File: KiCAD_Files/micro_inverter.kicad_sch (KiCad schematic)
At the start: 47 parts, among them J1 Conn_01x01, J103 B2B-EH-A(LF)(SN), J104 B2B-EH-A(LF)(SN), J105 B2B-EH-A(LF)(SN), J2 Conn_01x01, J3 Conn_01x01, J7 Conn_01x01, J8 Conn_01x01, K1 G2RL-1A-H, K2 G2RL-2A, Q501 IPD60R210PFD7SAUMA1, Q502 IPD60R210PFD7SAUMA1, Q503 IPD60R210PFD7SAUMA1, Q504 IPD60R210PFD7SAUMA1, Q505 IPD60R210PFD7SAUMA1, Q506 IPD60R210PFD7SAUMA1, Q507 IPD60R210PFD7SAUMA1, Q508 IPD60R210PFD7SAUMA1, Q509 IPD60R210PFD7SAUMA1, Q510 IPD60R210PFD7SAUMA1, Q511 IPD60R210PFD7SAUMA1, Q512 IPD60R210PFD7SAUMA1, T1 Transformer_1P_1S

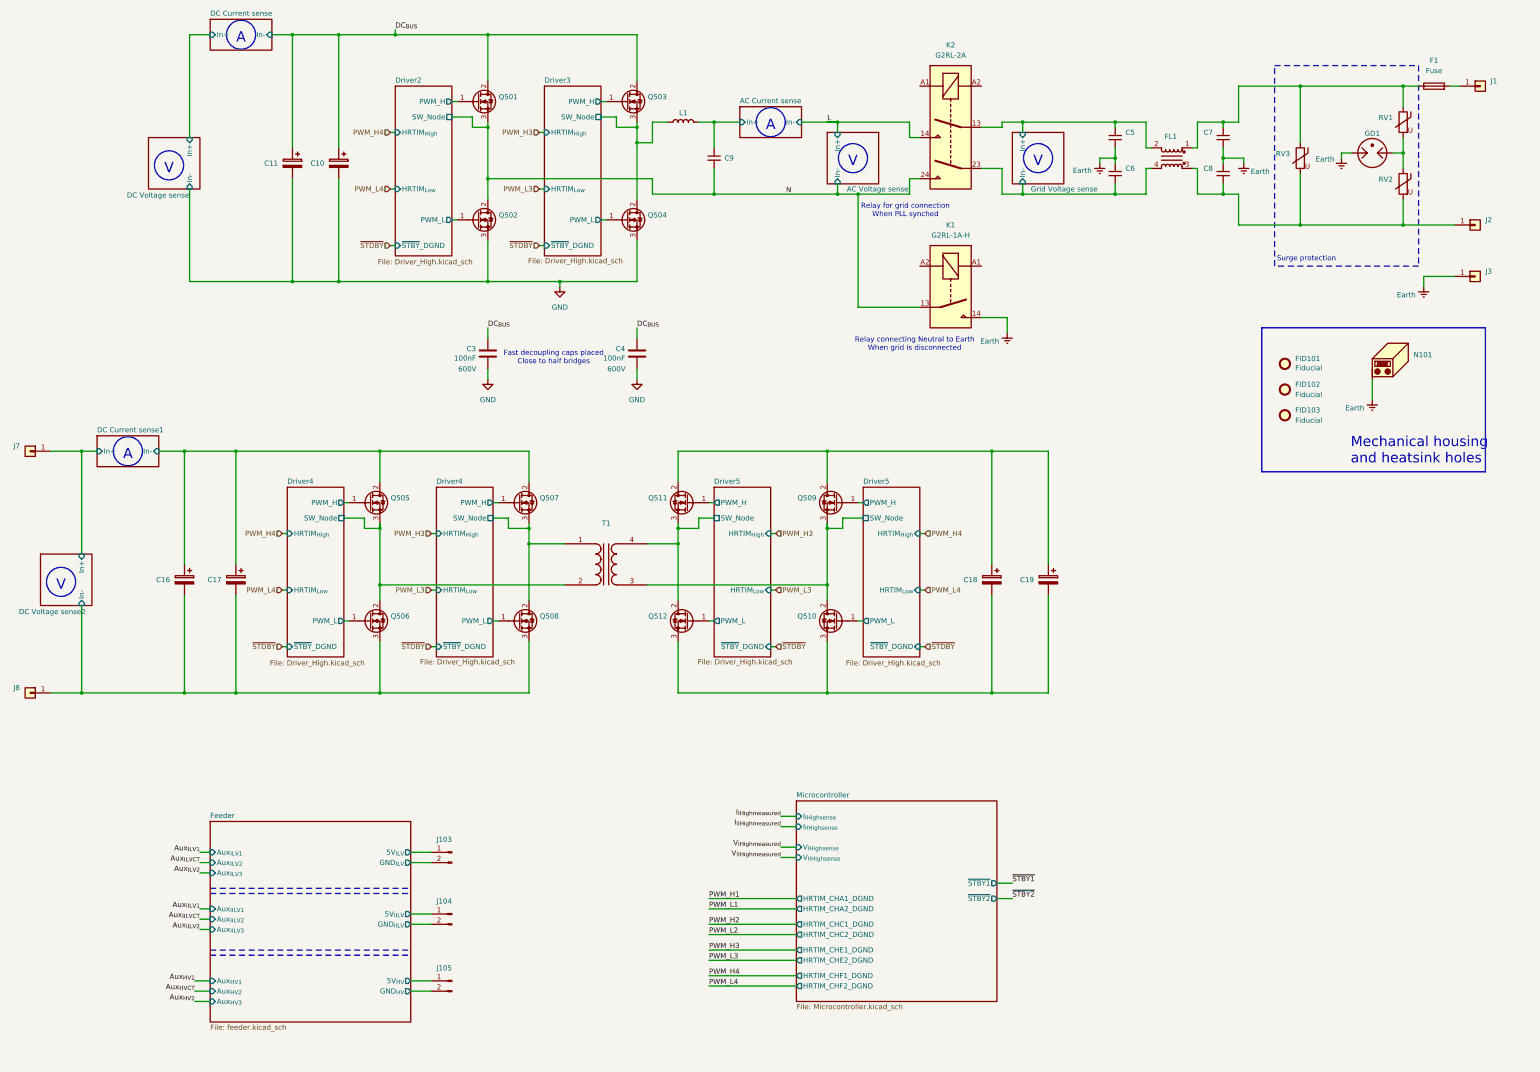
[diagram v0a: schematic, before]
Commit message: Changed the architecture from DAB to full-bridge. Added low side feeder.
Signed-off-by: Jean Alinei <jean.alinei@owntech.org>
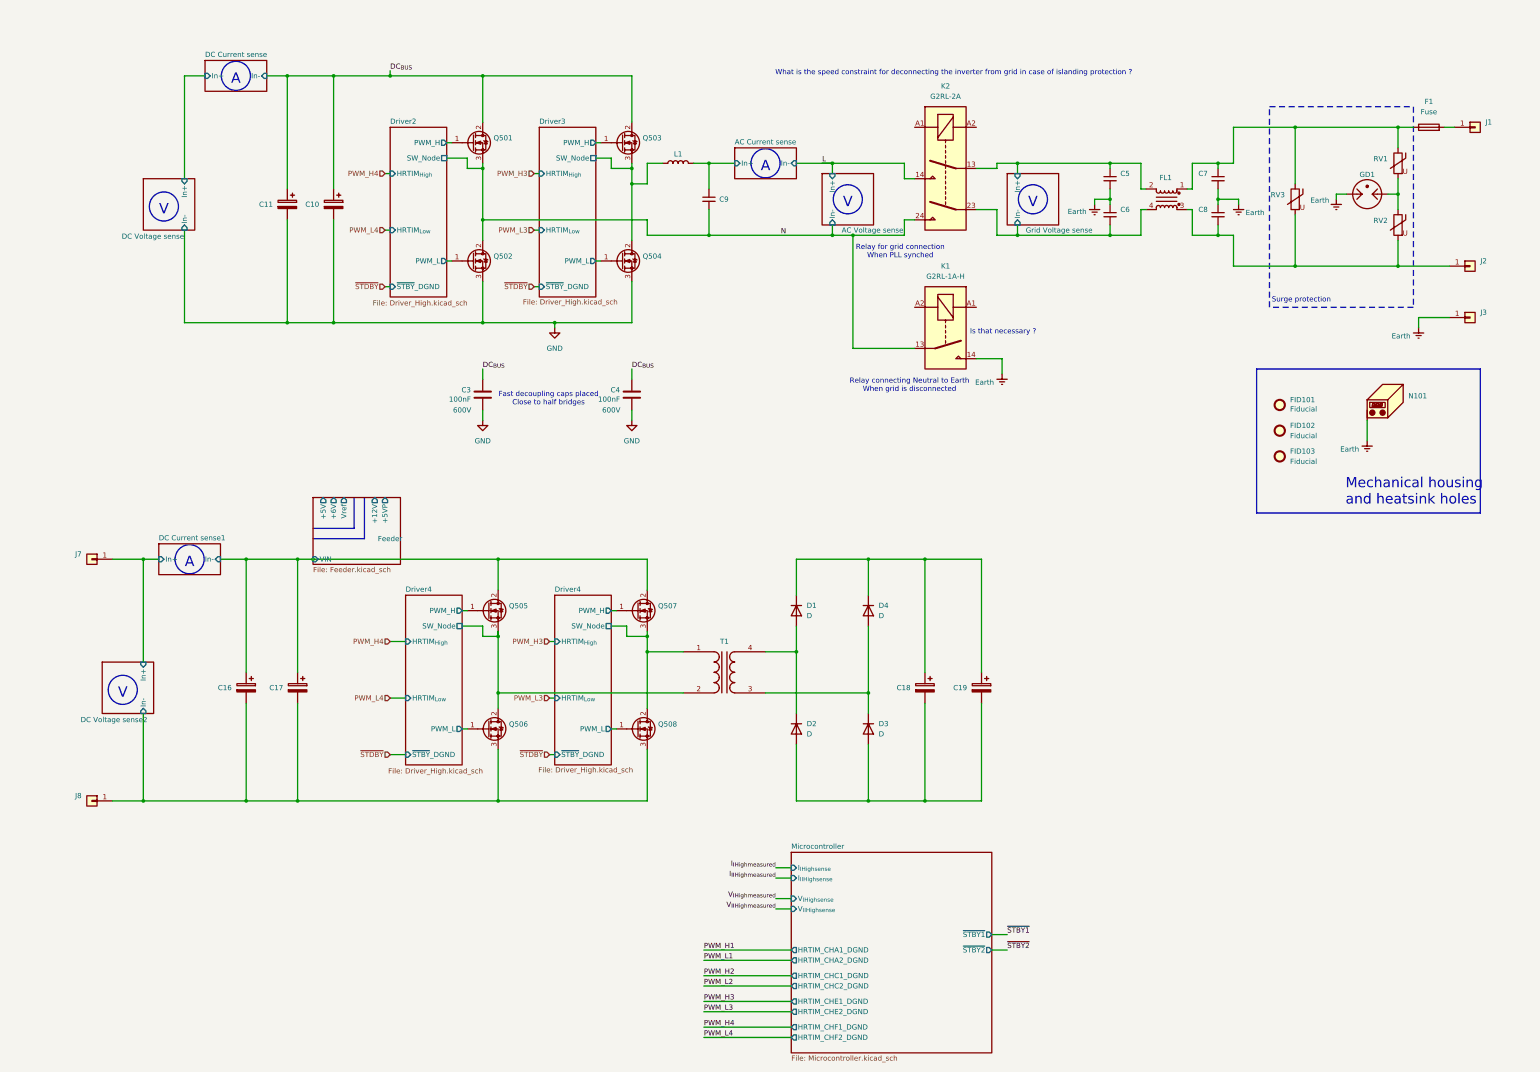
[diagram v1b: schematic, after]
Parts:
- removed J103, J104, J105: B2B-EH-A(LF)(SN), Connector_JST:JST_EH_B2B-EH-A_1x02_P2.50mm_Vertical, symbol Connector:Conn_01x02_Male
- removed Q509, Q510, Q511, Q512: IPD60R210PFD7SAUMA1, Package_TO_SOT_SMD:TO-252-2, symbol Transistor_FET:QM6006D
- added D1, D2, D3, D4: D, symbol Device:D
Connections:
- net Driver4/PWM_H is gone; now on net Driver4/PWM_H: Q505.1 (G)
- net Driver4/PWM_L is gone; now on net Driver4/PWM_L: Q508.1 (G)
- net Driver4/SW_Node is gone; now on net Driver4/SW_Node: Q507.3 (S), Q508.2 (D), T1.1 (AA)
- net Driver4/PWM_H: no longer Q507.1 (G)
- net Driver4/PWM_L: no longer Q506.1 (G)
- net Driver4/SW_Node: no longer Q505.3 (S), Q506.2 (D), T1.2 (AB)
- net at C18.1, C19.1: now also D1.1 (K), D4.1 (K)
- net at C18.2, C19.2: now also D2.2 (A), D3.2 (A)
- net Driver5/SW_Node: no longer names the net of T1.3 (SA)
- net Driver5/SW_Node: now also D3.1 (K), D4.2 (A)
- net Driver5/SW_Node: no longer names the net of T1.4 (SB)
- net Driver5/SW_Node: now also D1.2 (A), D2.1 (K)
- new net Driver4/PWM_H: Q507.1 (G)
- new net Driver4/PWM_L: Q506.1 (G)
- new net Driver4/SW_Node: Q505.3 (S), Q506.2 (D), T1.2 (AB)
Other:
- removed sheet Driver5
- sheet Feeder: file feeder.kicad_sch -> Feeder.kicad_sch
- sheet Feeder ports: added +12V, +5V, +5VP, +6V, VIN, Vref; removed 5V_{HV}, 5V_{IILV}, 5V_{ILV}, Aux_{HV1}, Aux_{HV2}, Aux_{HV3}, Aux_{IILV1}, Aux_{IILV2}, Aux_{IILV3}, Aux_{ILV1}, Aux_{ILV2}, Aux_{ILV3}, GND_{HV}, GND_{IILV}, GND_{ILV}
- note added: "Is that necessary ?"
- note added: "What is the speed constraint for deconnecting the inverter from grid in case of islanding protection ?"
- moved on the sheet: C10, C11, C16, C17, C18, C19, C3, C4, C5, C6, C7, C8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

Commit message: Schematic close to completion.
Signed-off-by: Jean Alinei <jean.alinei@owntech.org>
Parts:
- removed C10, C11, C16, C17, C18, C19: C_Polarized, symbol Device:C_Polarized
- removed D1, D2, D3, D4: D, symbol Device:D
- removed K1: G2RL-1A-H, Relay_THT:Relay_SPST_Omron_G2RL-1A, symbol Relay:G2RL-1A-H
- removed Q501, Q502, Q503, Q504, Q507, Q508: IPD60R210PFD7SAUMA1, Package_TO_SOT_SMD:TO-252-2, symbol Transistor_FET:QM6006D
- added C1: 220nF, symbol Device:C_Small
- added C11: 110uF, symbol Device:C
- added C18, C19, C53, C54, C55, C56, C57, C58: C_Small, symbol Device:C_Small
- added C51, C52, C60, C61, C62, C63, C64, C65: C, symbol Device:C
- added D1, D2, D3, D4: D_Schottky, symbol Device:D_Schottky
- added F2: Fuse, symbol Device:Fuse
- added FB1, FB2: 400@100MHz, symbol Device:FerriteBead_Small
- added L2: 330uH, symbol Device:L
- added L3, L4: 100uH, symbol Device:L
- added L5, L9: 33uH, symbol Device:L
- added Q3, Q7, Q8, Q9: ~, symbol Symbols:CID12N65D
- added Q4, Q5: IPD60R210PFD7SAUMA1, Package_TO_SOT_SMD:TO-252-2, symbol Transistor_FET:QM6006D
- added R1: 6.8R, symbol Device:R_Small
- added R31, R32, R33, R34: R_Small, symbol Device:R_Small
- added T3: Transformer_1P_1S, symbol Device:Transformer_1P_1S
- C3, C4: value 100nF -> 1nF
- C9: value C_Small -> 220nF
- L1: value L -> 330uH
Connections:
- net Driver4/PWM_H is gone; now on net Driver4/PWM_H: Q505.1 (G)
- net Driver4/SW_Node is gone; now on net Driver4/SW_Node: T1.1 (AA)
- net AC Current sense/In+: now also K2.23; no longer C9.1, L1.2
- net DC Current sense1/In-: now also L9.1; no longer Q505.2 (D)
- net DC Voltage sense2/In-: now also C61.2, C63.2, Q5.3 (S)
- net Driver4/SW_Node: now also L5.2; no longer T1.2 (AB)
- net GND: now also C11.2, C52.2, C55.2, C56.2, C57.2, C58.2, C65.2, D3.2 (A), D4.2 (A), Q7. (S), Q8. (S)
- net Grid Voltage sense/In+: now also F1.1, RV1.1, RV3.1; no longer C5.1, FL1.2
- net L: now also C5.1, C7.1, FL1.1, FL1.2, L3.2
- net N: now also C6.2, C8.2, FL1.3, FL1.4, L4.2; no longer C9.2
- net at T1.3 (SA): now also C51.2, C52.1
- net at T1.4 (SB): now also D1.2 (A), D3.1 (K)
- net Driver3/SW_Node: no longer names the net of L1.1
- net Driver3/SW_Node: now also FB1.2
- removed net Grid Voltage sense/In-: C6.2, FL1.4, K2.23
- new net: C57.1, Q7. (S)
- new net: Q7. (S), R33.1
- new net: Q7. (S), R33.2
- new net: C60.1, Q505.2 (D)
- new net: C60.2, C61.1, T1.2 (AB)
- new net: FB2.2, L2.1
- new net: C1.2, L2.2, L4.1, R1.2
- new net: C1.1, C9.1, L1.2, L3.1
- new net: C9.2, R1.1
- new net: C55.1, Q8. (S)
- new net: Q8. (S), R32.1
- new net: Q8. (S), R32.2
- new net: C64.2, C65.1, T3.3 (SA)
- new net: F2.2, J2.1 (Pin_1)
- new net: C62.2, C63.1, T3.2 (AB)
- new net: C62.1, Q4.2 (D)
- new net: D2.2 (A), D4.1 (K), T3.4 (SB)
- new net: Q3. (S), R34.1
- new net: Q3. (S), R34.2
- new net: C19.1, Q3. (S)
- new net: C53.1, Q9. (S)
- new net: Q9. (S), R31.1
- new net: Q9. (S), R31.2
- new net +12V_{HV}: C56.1, C58.1, Q7. (S), Q8. (S)
- new net +12V_{SN1}: C54.1, Q9. (S)
- new net +12V_{SN2}: C18.1, Q3. (S)
- new net AC Current sense/In-: F2.1, RV2.2, RV3.2
- new net DC Current sense2/In-: L5.1
- new net Driver6/PWM_H: Q4.1 (G)
- new net Driver6/PWM_L: Q5.1 (G)
- new net Driver6/SW_Node: L9.2, Q4.3 (S), Q5.2 (D), T3.1 (AA)
- new net HV_{BUS}: C11.1, C51.1, C64.1, D1.1 (K), D2.1 (K), Q3. (S), Q9. (S)
- new net SN1: C53.2, C54.2, FB2.1, Q8. (S), Q9. (S)
- new net SN2: C18.2, C19.2, FB1.1, Q3. (S), Q7. (S)
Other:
- removed sheet AC Voltage sense
- removed sheet DC Current sense
- removed sheet Driver2
- removed sheet Driver3
- added sheet DC Current sense2 (current.kicad_sch)
- added sheet Driver6 (Driver_High.kicad_sch)
- note added: "Aluminum PCB"
- note added: "Surge protection PCB"
- note removed: "Is that necessary ?"
- note removed: "Relay connecting Neutral to Earth When grid is disconnected"
- note removed: "Surge protection"
- moved on the sheet: C3, C4, C5, C6, C7, C8, C9, F1, FID101, FID102, FID103, FL1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
